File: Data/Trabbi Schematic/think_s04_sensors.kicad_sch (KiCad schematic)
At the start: 4 parts, among them SW1 Gear Selector (D7), U1 Motor Position Sensor (E05), U2 DC/DC High Effect Ref

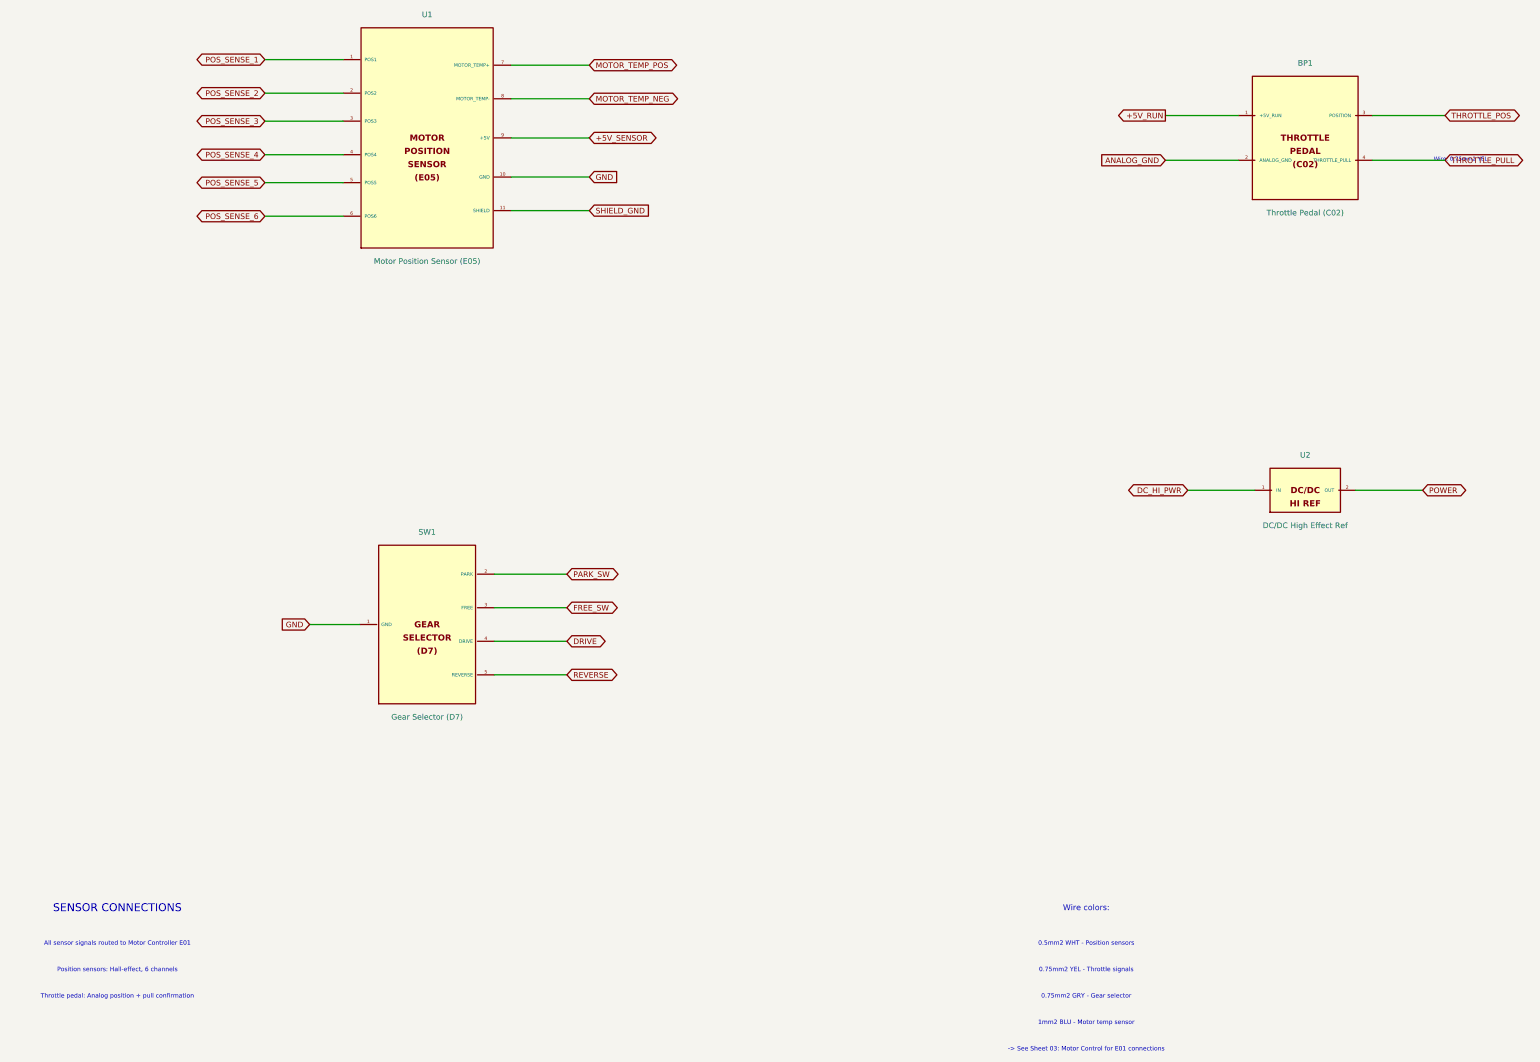
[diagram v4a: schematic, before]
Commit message: Add cross-sheet reference annotations to global labels
- Track all global label positions per sheet during build
- After building all sheets, annotate each global label with
  "→S01,S03,..." text showing which other sheets share the net
- 60 cross-sheet nets identified and annotated
- Two-pass build: 1) build all sheets 2) add cross-refs + save
- Text placed near label in 0.8mm font, offset to avoid overlap

Co-Authored-By: Claude Opus 4.6 <noreply@anthropic.com>
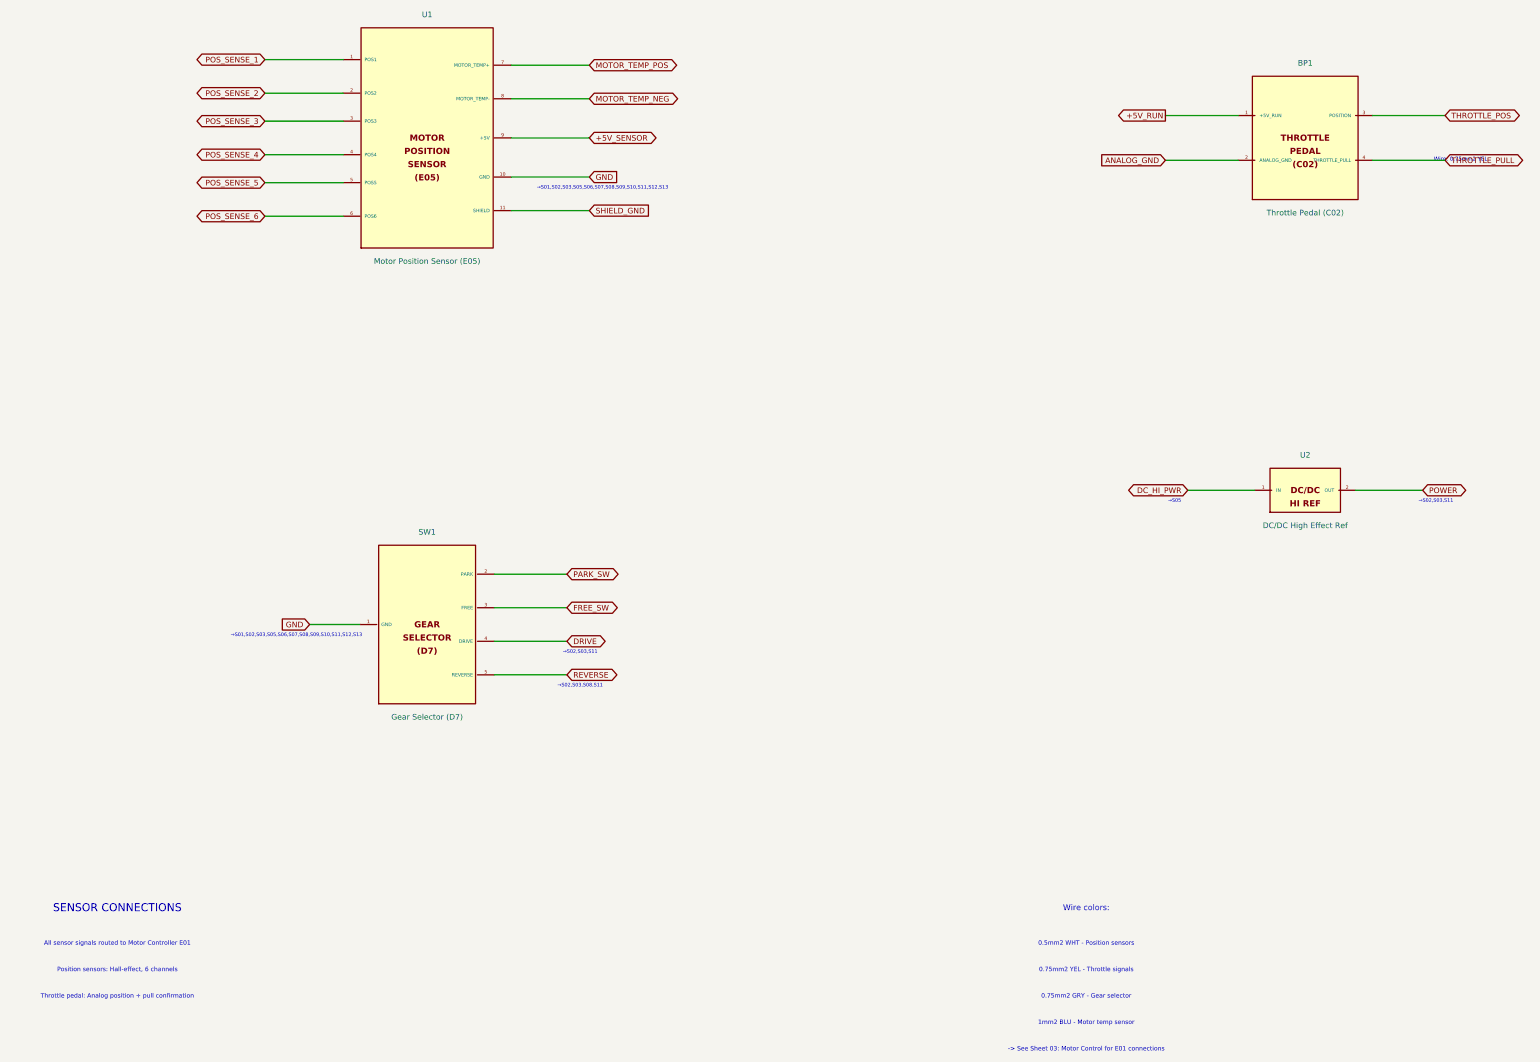
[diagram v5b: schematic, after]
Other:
- note added: "→S01,S02,S03,S05,S06,S07,S08,S09,S10,S11,S12,S13"
- note added: "→S02,S03,S08,S11"
- note added: "→S02,S03,S11"
- note added: "→S05"
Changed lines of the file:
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@@
     (effects (font (size 1.000 1.000)))
+  )
+  (text "→S01,S02,S03,S05,S06,S07,S08,S09,S10,S11,S12,S13" (at 140.160 91.400 0)
+    (effects (font (size 0.800 0.800)))
+  )
+  (text "→S01,S02,S03,S05,S06,S07,S08,S09,S10,S11,S12,S13" (at 70.660 193.000 0)
+    (effects (font (size 0.800 0.800)))
+  )
+  (text "→S02,S03,S11" (at 135.080 196.810 0)
+    (effects (font (size 0.800 0.800)))
+  )
+  (text "→S02,S03,S08,S11" (at 135.080 204.430 0)
+    (effects (font (size 0.800 0.800)))
+  )
+  (text "→S05" (at 270.050 162.520 0)
+    (effects (font (size 0.800 0.800)))
+  )
+  (text "→S02,S03,S11" (at 329.390 162.520 0)
+    (effects (font (size 0.800 0.800)))
   )
   (symbol_instances)

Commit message: Fix label text justification for KiCad 9
Add (justify left) to all label and global_label effects.
KiCad 9 requires explicit text justification — without it,
label text is mispositioned relative to the label shape.

Co-Authored-By: Claude Opus 4.6 <noreply@anthropic.com>
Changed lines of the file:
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@@
   )
   (global_label "POS_SENSE_1" (shape bidirectional) (at 63.500 62.230 180)
-    (effects (font (size 1.27 1.27)))
+    (effects (font (size 1.27 1.27)) (justify left))
     (property "Intersheetrefs" "${INTERSHEET_REFS}" (at 63.500 62.230 0)
       (effects (font (size 1.27 1.27)) hide)
@@
   )
   (global_label "POS_SENSE_2" (shape bidirectional) (at 63.500 69.850 180)
-    (effects (font (size 1.27 1.27)))
+    (effects (font (size 1.27 1.27)) (justify left))
     (property "Intersheetrefs" "${INTERSHEET_REFS}" (at 63.500 69.850 0)
       (effects (font (size 1.27 1.27)) hide)
@@
   )
   (global_label "POS_SENSE_3" (shape bidirectional) (at 63.500 76.200 180)
-    (effects (font (size 1.27 1.27)))
+    (effects (font (size 1.27 1.27)) (justify left))
     (property "Intersheetrefs" "${INTERSHEET_REFS}" (at 63.500 76.200 0)
       (effects (font (size 1.27 1.27)) hide)
@@
   )
   (global_label "POS_SENSE_4" (shape bidirectional) (at 63.500 83.820 180)
-    (effects (font (size 1.27 1.27)))
+    (effects (font (size 1.27 1.27)) (justify left))
     (property "Intersheetrefs" "${INTERSHEET_REFS}" (at 63.500 83.820 0)
       (effects (font (size 1.27 1.27)) hide)
@@
   )
   (global_label "POS_SENSE_5" (shape bidirectional) (at 63.500 90.170 180)
-    (effects (font (size 1.27 1.27)))
+    (effects (font (size 1.27 1.27)) (justify left))
     (property "Intersheetrefs" "${INTERSHEET_REFS}" (at 63.500 90.170 0)
       (effects (font (size 1.27 1.27)) hide)
@@
   )
   (global_label "POS_SENSE_6" (shape bidirectional) (at 63.500 97.790 180)
-    (effects (font (size 1.27 1.27)))
+    (effects (font (size 1.27 1.27)) (justify left))
     (property "Intersheetrefs" "${INTERSHEET_REFS}" (at 63.500 97.790 0)
       (effects (font (size 1.27 1.27)) hide)
@@
   )
   (global_label "MOTOR_TEMP_POS" (shape bidirectional) (at 137.160 63.500 0)
-    (effects (font (size 1.27 1.27)))
+    (effects (font (size 1.27 1.27)) (justify left))
     (property "Intersheetrefs" "${INTERSHEET_REFS}" (at 137.160 63.500 0)
       (effects (font (size 1.27 1.27)) hide)
@@
   )
   (global_label "MOTOR_TEMP_NEG" (shape bidirectional) (at 137.160 71.120 0)
-    (effects (font (size 1.27 1.27)))
+    (effects (font (size 1.27 1.27)) (justify left))
     (property "Intersheetrefs" "${INTERSHEET_REFS}" (at 137.160 71.120 0)
       (effects (font (size 1.27 1.27)) hide)
@@
   )
   (global_label "+5V_SENSOR" (shape bidirectional) (at 137.160 80.010 0)
-    (effects (font (size 1.27 1.27)))
+    (effects (font (size 1.27 1.27)) (justify left))
     (property "Intersheetrefs" "${INTERSHEET_REFS}" (at 137.160 80.010 0)
       (effects (font (size 1.27 1.27)) hide)
@@
   )
   (global_label "GND" (shape input) (at 137.160 88.900 0)
-    (effects (font (size 1.27 1.27)))
+    (effects (font (size 1.27 1.27)) (justify left))
     (property "Intersheetrefs" "${INTERSHEET_REFS}" (at 137.160 88.900 0)
       (effects (font (size 1.27 1.27)) hide)
@@
   )
   (global_label "SHIELD_GND" (shape input) (at 137.160 96.520 0)
-    (effects (font (size 1.27 1.27)))
+    (effects (font (size 1.27 1.27)) (justify left))
     (property "Intersheetrefs" "${INTERSHEET_REFS}" (at 137.160 96.520 0)
       (effects (font (size 1.27 1.27)) hide)
@@
   )
   (global_label "PARK_SW" (shape bidirectional) (at 132.080 179.070 0)
-    (effects (font (size 1.27 1.27)))
+    (effects (font (size 1.27 1.27)) (justify left))
     (property "Intersheetrefs" "${INTERSHEET_REFS}" (at 132.080 179.070 0)
       (effects (font (size 1.27 1.27)) hide)
@@
   )
   (global_label "FREE_SW" (shape bidirectional) (at 132.080 186.690 0)
-    (effects (font (size 1.27 1.27)))
+    (effects (font (size 1.27 1.27)) (justify left))
     (property "Intersheetrefs" "${INTERSHEET_REFS}" (at 132.080 186.690 0)
       (effects (font (size 1.27 1.27)) hide)
@@
   )
   (global_label "DRIVE" (shape bidirectional) (at 132.080 194.310 0)
-    (effects (font (size 1.27 1.27)))
+    (effects (font (size 1.27 1.27)) (justify left))
     (property "Intersheetrefs" "${INTERSHEET_REFS}" (at 132.080 194.310 0)
       (effects (font (size 1.27 1.27)) hide)
@@
   )
   (global_label "REVERSE" (shape bidirectional) (at 132.080 201.930 0)
-    (effects (font (size 1.27 1.27)))
+    (effects (font (size 1.27 1.27)) (justify left))
     (property "Intersheetrefs" "${INTERSHEET_REFS}" (at 132.080 201.930 0)
       (effects (font (size 1.27 1.27)) hide)
@@
   )
   (global_label "GND" (shape input) (at 73.660 190.500 180)
-    (effects (font (size 1.27 1.27)))
+    (effects (font (size 1.27 1.27)) (justify left))
     (property "Intersheetrefs" "${INTERSHEET_REFS}" (at 73.660 190.500 0)
       (effects (font (size 1.27 1.27)) hide)
@@
   )
   (global_label "+5V_RUN" (shape output) (at 267.970 74.930 180)
-    (effects (font (size 1.27 1.27)))
+    (effects (font (size 1.27 1.27)) (justify left))
     (property "Intersheetrefs" "${INTERSHEET_REFS}" (at 267.970 74.930 0)
       (effects (font (size 1.27 1.27)) hide)
@@
   )
   (global_label "ANALOG_GND" (shape input) (at 267.970 85.090 180)
-    (effects (font (size 1.27 1.27)))
+    (effects (font (size 1.27 1.27)) (justify left))
     (property "Intersheetrefs" "${INTERSHEET_REFS}" (at 267.970 85.090 0)
       (effects (font (size 1.27 1.27)) hide)
@@
   )
   (global_label "THROTTLE_POS" (shape bidirectional) (at 331.470 74.930 0)
-    (effects (font (size 1.27 1.27)))
+    (effects (font (size 1.27 1.27)) (justify left))
     (property "Intersheetrefs" "${INTERSHEET_REFS}" (at 331.470 74.930 0)
       (effects (font (size 1.27 1.27)) hide)
@@
   )
   (global_label "THROTTLE_PULL" (shape bidirectional) (at 331.470 85.090 0)
-    (effects (font (size 1.27 1.27)))
+    (effects (font (size 1.27 1.27)) (justify left))
     (property "Intersheetrefs" "${INTERSHEET_REFS}" (at 331.470 85.090 0)
       (effects (font (size 1.27 1.27)) hide)
@@
   )
   (global_label "DC_HI_PWR" (shape bidirectional) (at 273.050 160.020 180)
-    (effects (font (size 1.27 1.27)))
+    (effects (font (size 1.27 1.27)) (justify left))
     (property "Intersheetrefs" "${INTERSHEET_REFS}" (at 273.050 160.020 0)
       (effects (font (size 1.27 1.27)) hide)
@@
   )
   (global_label "POWER" (shape bidirectional) (at 326.390 160.020 0)
-    (effects (font (size 1.27 1.27)))
+    (effects (font (size 1.27 1.27)) (justify left))
     (property "Intersheetrefs" "${INTERSHEET_REFS}" (at 326.390 160.020 0)
       (effects (font (size 1.27 1.27)) hide)

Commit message: Relay symbol for flasher, label justify set to auto
- Flasher Relay (Think:FLASHER_RELAY) now has coil+switch graphics
  matching the standard relay symbol style
- All relays (SPST, SPDT, Flasher) use consistent coil+switch body
- Remove (justify left) from all label and global_label effects —
  KiCad 9 auto-determines text alignment based on label orientation

Co-Authored-By: Claude Opus 4.6 <noreply@anthropic.com>
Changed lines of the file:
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@@
   )
   (global_label "POS_SENSE_1" (shape bidirectional) (at 63.500 62.230 180)
-    (effects (font (size 1.27 1.27)) (justify left))
+    (effects (font (size 1.27 1.27)))
     (property "Intersheetrefs" "${INTERSHEET_REFS}" (at 63.500 62.230 0)
       (effects (font (size 1.27 1.27)) hide)
@@
   )
   (global_label "POS_SENSE_2" (shape bidirectional) (at 63.500 69.850 180)
-    (effects (font (size 1.27 1.27)) (justify left))
+    (effects (font (size 1.27 1.27)))
     (property "Intersheetrefs" "${INTERSHEET_REFS}" (at 63.500 69.850 0)
       (effects (font (size 1.27 1.27)) hide)
@@
   )
   (global_label "POS_SENSE_3" (shape bidirectional) (at 63.500 76.200 180)
-    (effects (font (size 1.27 1.27)) (justify left))
+    (effects (font (size 1.27 1.27)))
     (property "Intersheetrefs" "${INTERSHEET_REFS}" (at 63.500 76.200 0)
       (effects (font (size 1.27 1.27)) hide)
@@
   )
   (global_label "POS_SENSE_4" (shape bidirectional) (at 63.500 83.820 180)
-    (effects (font (size 1.27 1.27)) (justify left))
+    (effects (font (size 1.27 1.27)))
     (property "Intersheetrefs" "${INTERSHEET_REFS}" (at 63.500 83.820 0)
       (effects (font (size 1.27 1.27)) hide)
@@
   )
   (global_label "POS_SENSE_5" (shape bidirectional) (at 63.500 90.170 180)
-    (effects (font (size 1.27 1.27)) (justify left))
+    (effects (font (size 1.27 1.27)))
     (property "Intersheetrefs" "${INTERSHEET_REFS}" (at 63.500 90.170 0)
       (effects (font (size 1.27 1.27)) hide)
@@
   )
   (global_label "POS_SENSE_6" (shape bidirectional) (at 63.500 97.790 180)
-    (effects (font (size 1.27 1.27)) (justify left))
+    (effects (font (size 1.27 1.27)))
     (property "Intersheetrefs" "${INTERSHEET_REFS}" (at 63.500 97.790 0)
       (effects (font (size 1.27 1.27)) hide)
@@
   )
   (global_label "MOTOR_TEMP_POS" (shape bidirectional) (at 137.160 63.500 0)
-    (effects (font (size 1.27 1.27)) (justify left))
+    (effects (font (size 1.27 1.27)))
     (property "Intersheetrefs" "${INTERSHEET_REFS}" (at 137.160 63.500 0)
       (effects (font (size 1.27 1.27)) hide)
@@
   )
   (global_label "MOTOR_TEMP_NEG" (shape bidirectional) (at 137.160 71.120 0)
-    (effects (font (size 1.27 1.27)) (justify left))
+    (effects (font (size 1.27 1.27)))
     (property "Intersheetrefs" "${INTERSHEET_REFS}" (at 137.160 71.120 0)
       (effects (font (size 1.27 1.27)) hide)
@@
   )
   (global_label "+5V_SENSOR" (shape bidirectional) (at 137.160 80.010 0)
-    (effects (font (size 1.27 1.27)) (justify left))
+    (effects (font (size 1.27 1.27)))
     (property "Intersheetrefs" "${INTERSHEET_REFS}" (at 137.160 80.010 0)
       (effects (font (size 1.27 1.27)) hide)
@@
   )
   (global_label "GND" (shape input) (at 137.160 88.900 0)
-    (effects (font (size 1.27 1.27)) (justify left))
+    (effects (font (size 1.27 1.27)))
     (property "Intersheetrefs" "${INTERSHEET_REFS}" (at 137.160 88.900 0)
       (effects (font (size 1.27 1.27)) hide)
@@
   )
   (global_label "SHIELD_GND" (shape input) (at 137.160 96.520 0)
-    (effects (font (size 1.27 1.27)) (justify left))
+    (effects (font (size 1.27 1.27)))
     (property "Intersheetrefs" "${INTERSHEET_REFS}" (at 137.160 96.520 0)
       (effects (font (size 1.27 1.27)) hide)
@@
   )
   (global_label "PARK_SW" (shape bidirectional) (at 132.080 179.070 0)
-    (effects (font (size 1.27 1.27)) (justify left))
+    (effects (font (size 1.27 1.27)))
     (property "Intersheetrefs" "${INTERSHEET_REFS}" (at 132.080 179.070 0)
       (effects (font (size 1.27 1.27)) hide)
@@
   )
   (global_label "FREE_SW" (shape bidirectional) (at 132.080 186.690 0)
-    (effects (font (size 1.27 1.27)) (justify left))
+    (effects (font (size 1.27 1.27)))
     (property "Intersheetrefs" "${INTERSHEET_REFS}" (at 132.080 186.690 0)
       (effects (font (size 1.27 1.27)) hide)
@@
   )
   (global_label "DRIVE" (shape bidirectional) (at 132.080 194.310 0)
-    (effects (font (size 1.27 1.27)) (justify left))
+    (effects (font (size 1.27 1.27)))
     (property "Intersheetrefs" "${INTERSHEET_REFS}" (at 132.080 194.310 0)
       (effects (font (size 1.27 1.27)) hide)
@@
   )
   (global_label "REVERSE" (shape bidirectional) (at 132.080 201.930 0)
-    (effects (font (size 1.27 1.27)) (justify left))
+    (effects (font (size 1.27 1.27)))
     (property "Intersheetrefs" "${INTERSHEET_REFS}" (at 132.080 201.930 0)
       (effects (font (size 1.27 1.27)) hide)
@@
   )
   (global_label "GND" (shape input) (at 73.660 190.500 180)
-    (effects (font (size 1.27 1.27)) (justify left))
+    (effects (font (size 1.27 1.27)))
     (property "Intersheetrefs" "${INTERSHEET_REFS}" (at 73.660 190.500 0)
       (effects (font (size 1.27 1.27)) hide)
@@
   )
   (global_label "+5V_RUN" (shape output) (at 267.970 74.930 180)
-    (effects (font (size 1.27 1.27)) (justify left))
+    (effects (font (size 1.27 1.27)))
     (property "Intersheetrefs" "${INTERSHEET_REFS}" (at 267.970 74.930 0)
       (effects (font (size 1.27 1.27)) hide)
@@
   )
   (global_label "ANALOG_GND" (shape input) (at 267.970 85.090 180)
-    (effects (font (size 1.27 1.27)) (justify left))
+    (effects (font (size 1.27 1.27)))
     (property "Intersheetrefs" "${INTERSHEET_REFS}" (at 267.970 85.090 0)
       (effects (font (size 1.27 1.27)) hide)
@@
   )
   (global_label "THROTTLE_POS" (shape bidirectional) (at 331.470 74.930 0)
-    (effects (font (size 1.27 1.27)) (justify left))
+    (effects (font (size 1.27 1.27)))
     (property "Intersheetrefs" "${INTERSHEET_REFS}" (at 331.470 74.930 0)
       (effects (font (size 1.27 1.27)) hide)
@@
   )
   (global_label "THROTTLE_PULL" (shape bidirectional) (at 331.470 85.090 0)
-    (effects (font (size 1.27 1.27)) (justify left))
+    (effects (font (size 1.27 1.27)))
     (property "Intersheetrefs" "${INTERSHEET_REFS}" (at 331.470 85.090 0)
       (effects (font (size 1.27 1.27)) hide)
@@
   )
   (global_label "DC_HI_PWR" (shape bidirectional) (at 273.050 160.020 180)
-    (effects (font (size 1.27 1.27)) (justify left))
+    (effects (font (size 1.27 1.27)))
     (property "Intersheetrefs" "${INTERSHEET_REFS}" (at 273.050 160.020 0)
       (effects (font (size 1.27 1.27)) hide)
@@
   )
   (global_label "POWER" (shape bidirectional) (at 326.390 160.020 0)
-    (effects (font (size 1.27 1.27)) (justify left))
+    (effects (font (size 1.27 1.27)))
     (property "Intersheetrefs" "${INTERSHEET_REFS}" (at 326.390 160.020 0)
       (effects (font (size 1.27 1.27)) hide)
